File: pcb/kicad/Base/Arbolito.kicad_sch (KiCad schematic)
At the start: 68 parts, among them J1 Battery, J10 Conn_01x01, J11 Conn_01x01, J12 Conn_01x01, J13 Conn_01x01, J14 Conn_01x01, J2 Conn_01x06_Female, J3 Conn_01x01, J4 Conn_01x01, J5 Conn_01x01, J6 Conn_01x01, J7 Conn_01x01, J8 Conn_01x01, J9 Conn_01x01, P1 TYPE-C 16PIN 2MD(073), Q1 S8050, Q2 S8050, Q3 S8050, SW1 SW_DP3T, SW2 SW_Push, SW3 SW_Push, SW4 SW_Push, U1 NCP115AMX120TCG, U2 CH340C, U3 AP63205WU, U4 ESP-12F, U5 SHT31-DIS

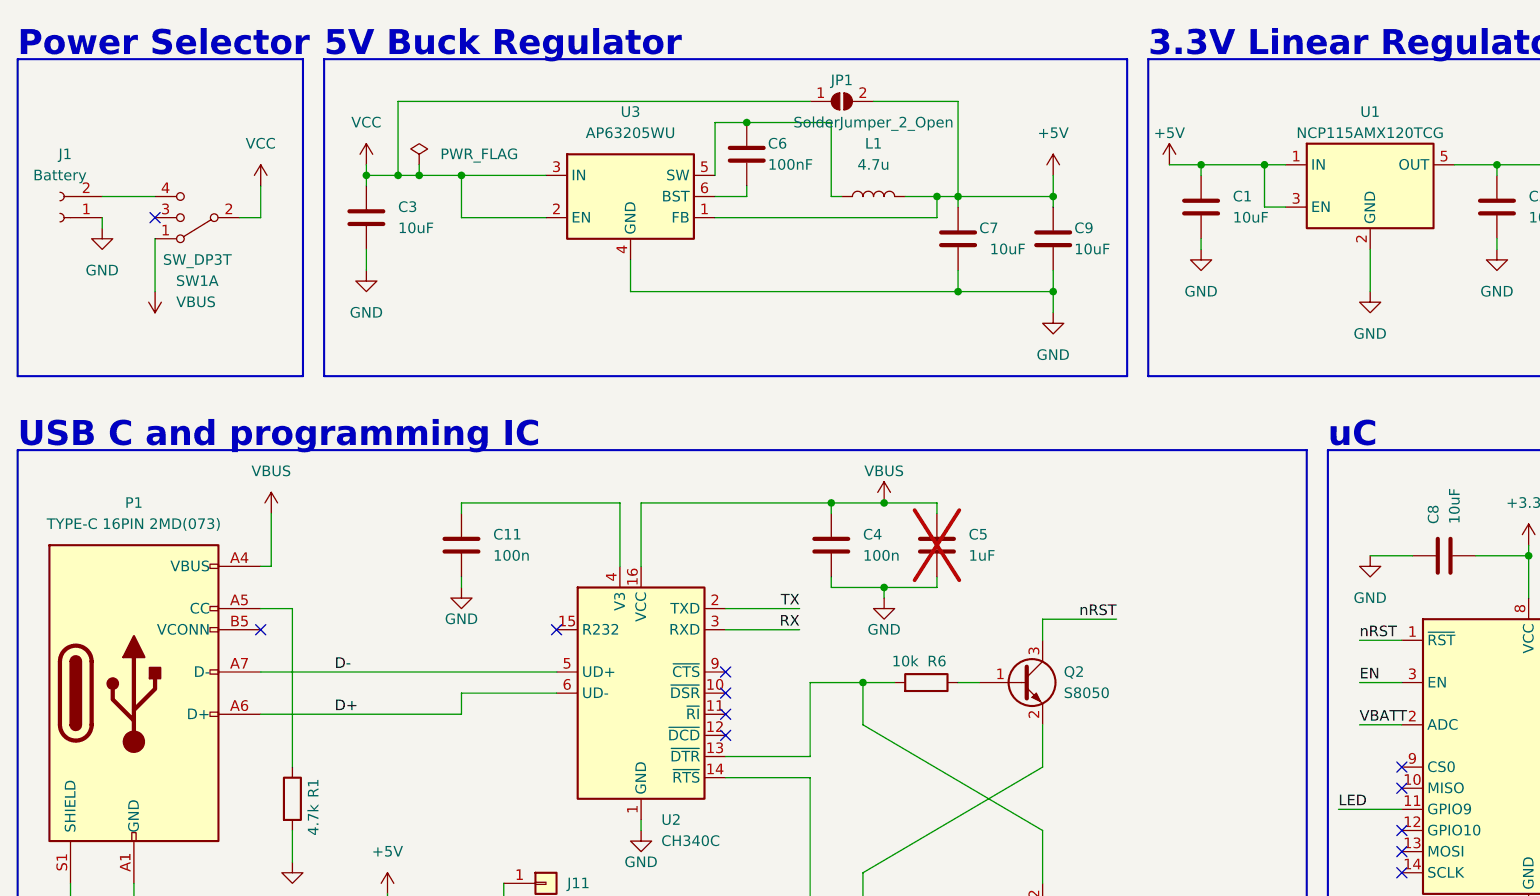
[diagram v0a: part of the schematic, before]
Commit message: USB Issues fixed
USB C Now reversible
USB C progamable
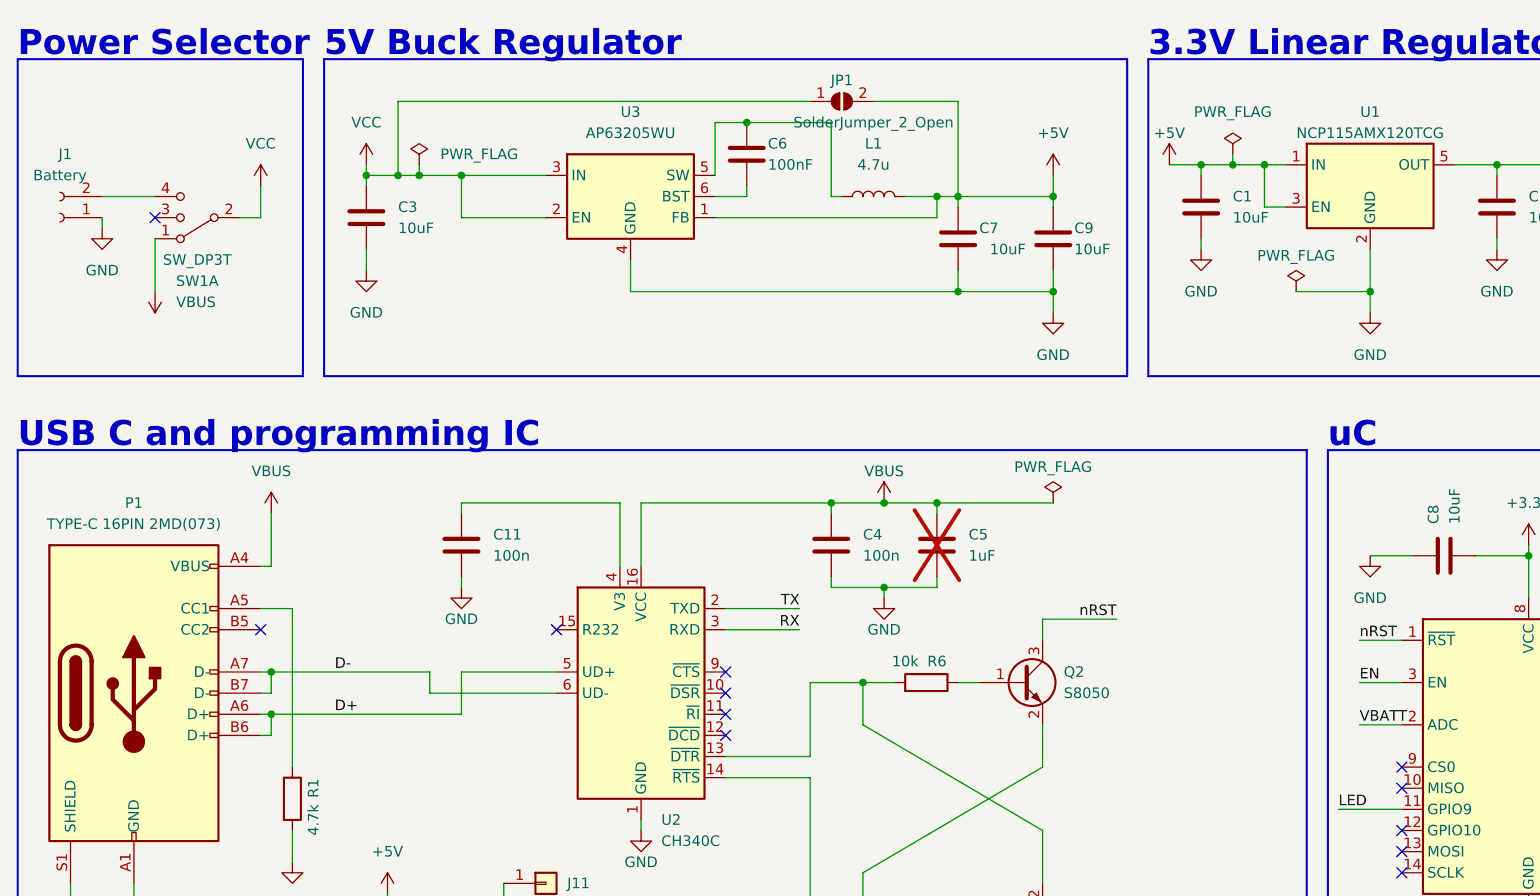
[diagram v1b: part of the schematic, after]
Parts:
- P1: symbol Connector:USB_C_Plug_USB2.0 -> Connector:USB_C_Receptacle_USB2.0_14P
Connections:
- net D+: now also P1.B6 (D+), U2.5 (UD+); no longer U2.6 (UD-)
- net D-: now also P1.B7 (D-), U2.6 (UD-); no longer U2.5 (UD+)
